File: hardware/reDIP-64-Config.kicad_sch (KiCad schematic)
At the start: 19 parts, among them J7 Conn_02x05_Odd_Even, SW1 KXT331LHS, U17 W957A8MFYA5I, U18 W25Q128JVPIM, U4 LFE5UM5G-25F-8MG285C

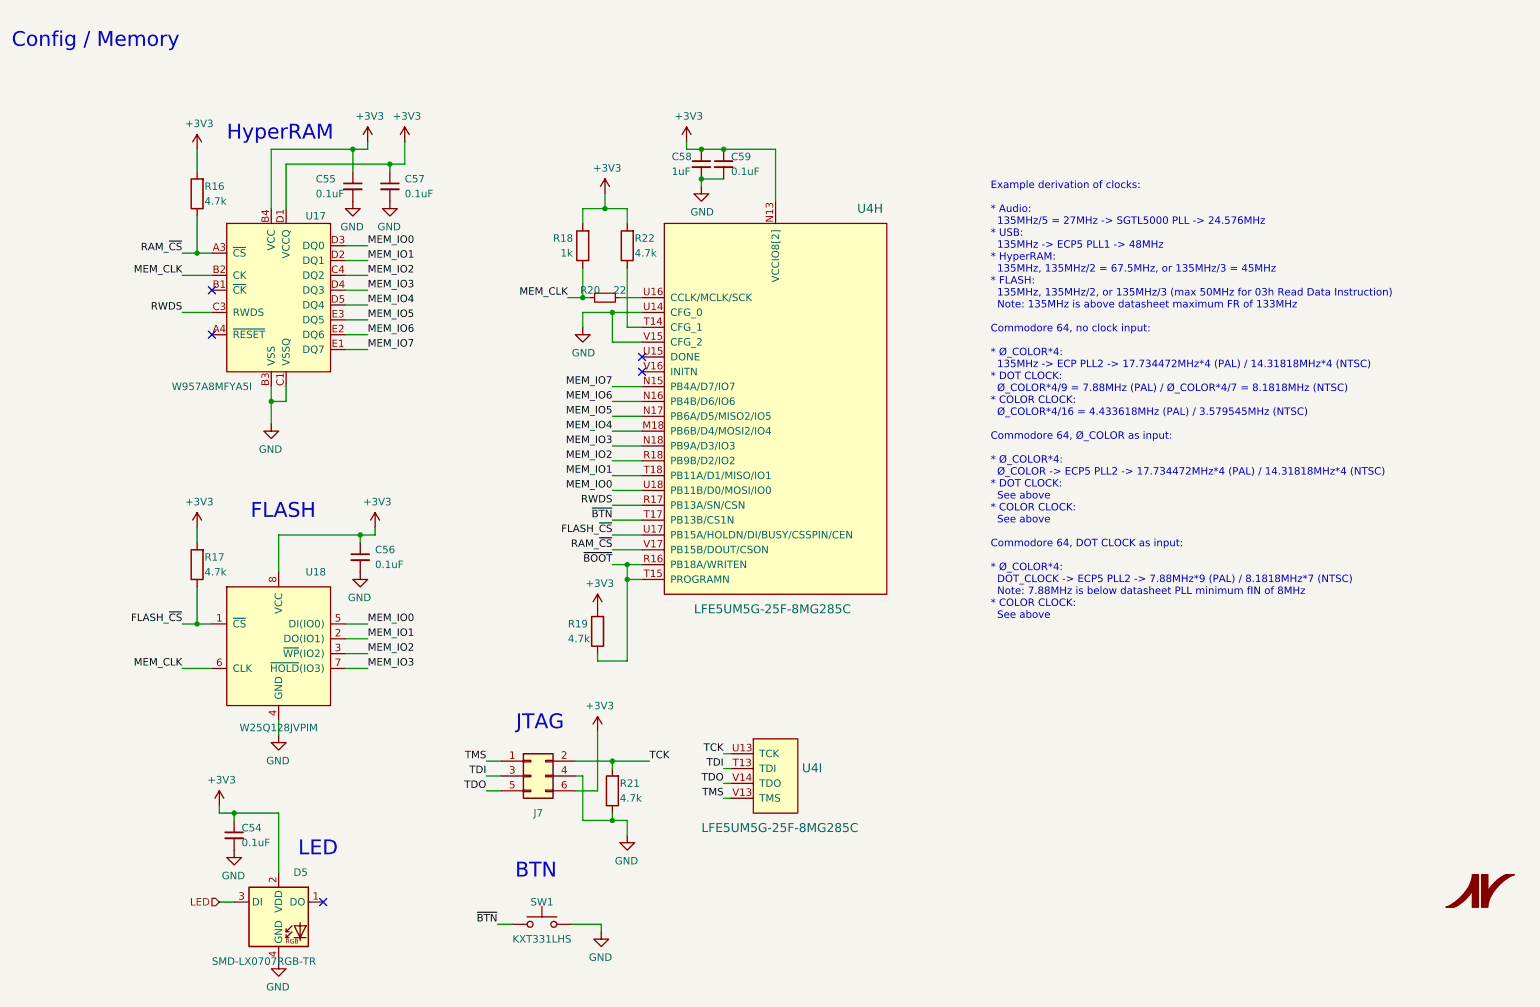
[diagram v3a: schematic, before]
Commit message: Revision 1.0
* USB receptacle replaced with GCT USB4080-03-A / HRO TYPE-C-31-M-05
* USB PD TCPC changed to PTN5110NHQ (FPF2286 has 15ms VBUS debounce time)
* Complete rework of power section
  - Over-voltage protection on VBUS (FPF2286 / FPF2495C)
  - Bidirectional VCC (2 x TPS22916)
  - Replaced EOLed buck converters with FAN53610 / FAN53611
  - Replaced EOLed LDO for ECP5 VCCAUX with NCP115AMX250TCG
  - Replaced LDO for SGTL5000 VDDA with 3.3V version
  - Added separate LDO for SGTL5000 VDDD, avoiding overvoltage on ECP5 VCC
* Bus switch changed to SN74CBT16211A, biased for level shifting
* Registered I/O for FLASH / HyperRAM clock
* Pin header changes:
  - Machined (round) pins for MOS6510 socket
  - Top only headers for additional I/O
  - Reworked pinout for VIC-II and SID
  - Removed 5V output (now available on bidirectional VCC)
  - Added GND for audio / 3.3V
  - Changed JTAG pinout to match Tag-Connect TC-LATTICE / TC-XILINX6
* Removed EXT_IN capacitors
* Button force changed from 240gf to 100gf
* Space for UL and date codes
* Black solder mask
* Silk screen updates
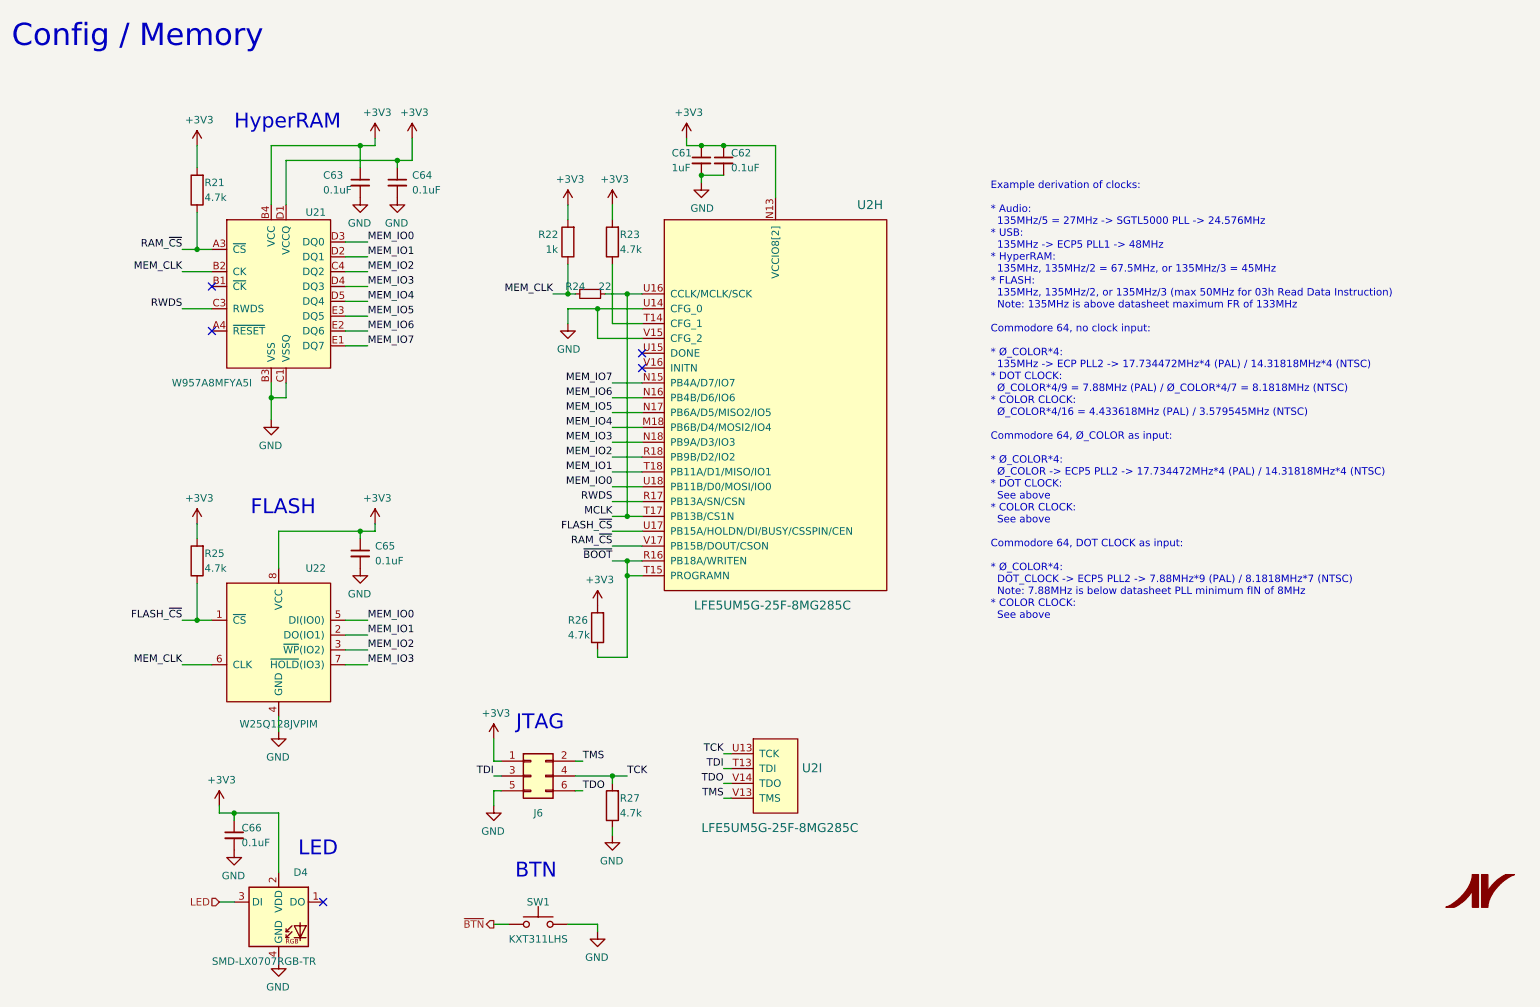
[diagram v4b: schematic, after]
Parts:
- J6: renamed from J7; Mfg Sullins -> (none); PN GRPB032VWVN-RC -> (none)
- R21: renamed from R16; PN ERJ-1GNJ472C -> ERJ1GNJ472C
- R22: renamed from R18; PN ERJ-1GNJ102C -> ERJ1GNF1001C
- R23: renamed from R22; PN ERJ-1GNJ472C -> ERJ1GNJ472C
- R24: renamed from R20; PN ERJ-1GNJ220C -> ERJ1GNJ220C
- R25: renamed from R17; PN ERJ-1GNJ472C -> ERJ1GNJ472C
- R26: renamed from R19; PN ERJ-1GNJ472C -> ERJ1GNJ472C
- R27: renamed from R21; PN ERJ-1GNJ472C -> ERJ1GNJ472C
- SW1: value KXT331LHS -> KXT311LHS; footprint Button_Switch_SMD:SW_SPST_CK_KXT3 -> CK:SW_SPST_CK_KXT3; PN KXT331LHS -> KXT311LHS
- renumbered C58 to C61, C59 to C62, C55 to C63, C57 to C64, C56 to C65, C54 to C66, D5 to D4, U4 to U2, U17 to U21, U18 to U22
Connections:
- net +3V3: now also J6.1 (Pin_1); no longer J6.6 (Pin_6)
- net GND: now also J6.5 (Pin_5); no longer J6.4 (Pin_4)
- net TCK: now also J6.4 (Pin_4); no longer J6.2 (Pin_2)
- net TDO: now also J6.6 (Pin_6); no longer J6.5 (Pin_5)
- net TMS: now also J6.2 (Pin_2); no longer J6.1 (Pin_1)
- net ~{BTN}: no longer U2.T17 (PB13B/CS1N)
- net MCLK: now reaches R24.1, U2.U16 (CCLK/MCLK/SCK)
- net MCLK: now also U2.T17 (PB13B/CS1N)
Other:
- moved on the sheet: C61, C62, C63, C64, C65, R21, R22, R23, R24, R25, R26, R27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

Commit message: Replaced socket pin headers with socket adapter
The socket adapter should hopefully *just* fit.
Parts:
- renumbered J6 to J5
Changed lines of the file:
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@@
   (symbol (lib_id "Connector_Generic:Conn_02x03_Odd_Even") (at 114.3 152.4 0) (unit 1)
     (in_bom yes) (on_board yes)
-    (property "Reference" "J6" (id 0) (at 115.57 158.75 0))
+    (property "Reference" "J5" (id 0) (at 115.57 158.75 0))
     (property "Value" "Conn_02x05_Odd_Even" (id 1) (at 115.57 144.1196 0)
       (effects (font (size 1.27 1.27)) hide)

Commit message: A few improvements
* Changed MCLK pullup to 4.7k
* A few pin swaps for cleaner routing
* Example pin headers in BOM
* Replaced reduced lifetime "mobile only" capacitors
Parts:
- C61: Notes 3.3V DC DERATED TO 1uF -> 3.3V DC DERATED TO 0.7uF; PN GRM035R60J475ME15D -> GRM033R60J225ME01D
- J5: Mfg (none) -> Sullins; PN (none) -> GRPB032VWVN-RC
- R22: value 1k -> 4.7k
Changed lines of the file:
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@@
   (title_block
     (title "reDIP 64")
-    (date "2022-04-10")
+    (date "2022-04-14")
     (rev "1.0")
     (company "Nimrod")
@@
   (symbol (lib_id "Device:R") (at 120.65 60.96 180) (unit 1)
     (in_bom yes) (on_board yes)
-    (property "Reference" "R22" (id 0) (at 115.57 59.69 0)
+    (property "Reference" "R22" (id 0) (at 121.92 59.69 0)
       (effects (font (size 1.27 1.27)) (justify right))
     )
-    (property "Value" "1k" (id 1) (at 116.84 62.23 0)
+    (property "Value" "4.7k" (id 1) (at 121.92 62.23 0)
       (effects (font (size 1.27 1.27)) (justify right))
     )
@@
       (effects (font (size 1.27 1.27)) hide)
     )
-    (property "Datasheet" "~" (id 3) (at 114.3 152.4 0)
-      (effects (font (size 1.27 1.27)) hide)
-    )
-    (property "Description" "CONN HDR SQ PIN 2x3 POS .050\" GOLD" (id 4) (at 114.3 152.4 0)
-      (effects (font (size 1.27 1.27)) hide)
-    )
-    (property "Mfg" "" (id 5) (at 114.3 152.4 0)
-      (effects (font (size 1.27 1.27)) hide)
-    )
-    (property "PN" "" (id 6) (at 114.3 152.4 0)
+    (property "Datasheet" "https://s3.amazonaws.com/catalogspreads-pdf/PAGE94-95%20.050%20MALE%20HDR%20ST%20RA%20SMT.pdf" (id 3) (at 114.3 152.4 0)
+      (effects (font (size 1.27 1.27)) hide)
+    )
+    (property "Description" "CONN HDR SQ PIN 2x3 POS .050\" GOLD MATING 3mm" (id 4) (at 114.3 152.4 0)
+      (effects (font (size 1.27 1.27)) hide)
+    )
+    (property "Mfg" "Sullins" (id 5) (at 114.3 152.4 0)
+      (effects (font (size 1.27 1.27)) hide)
+    )
+    (property "PN" "GRPB032VWVN-RC" (id 6) (at 114.3 152.4 0)
       (effects (font (size 1.27 1.27)) hide)
     )
@@
       (effects (font (size 1.27 1.27)) hide)
     )
-    (property "Datasheet" "https://www.murata.com/products/productdetail.aspx?partno=GRM035R60J475ME15D" (id 3) (at 143.51 46.99 0)
+    (property "Datasheet" "https://www.murata.com/products/productdetail.aspx?partno=GRM033R60J225ME01D" (id 3) (at 143.51 46.99 0)
       (effects (font (size 1.27 1.27)) hide)
     )
@@
       (effects (font (size 1.27 1.27)) hide)
     )
-    (property "PN" "GRM035R60J475ME15D" (id 5) (at 143.51 46.99 0)
-      (effects (font (size 1.27 1.27)) hide)
-    )
-    (property "Description" "CAP CER 4.7uF 6.3V 20% X5R 0201" (id 6) (at 143.51 46.99 0)
-      (effects (font (size 1.27 1.27)) hide)
-    )
-    (property "Notes" "3.3V DC DERATED TO 1uF" (id 7) (at 143.51 46.99 0)
-      (effects (font (size 1.27 1.27)) hide)
-    )
+    (property "PN" "GRM033R60J225ME01D" (id 5) (at 143.51 46.99 0)
+      (effects (font (size 1.27 1.27)) hide)
+    )
+    (property "Description" "CAP CER 2.2uF 6.3V 20% X5R 0201" (id 6) (at 143.51 46.99 0)
+      (effects (font (size 1.27 1.27)) hide)
+    )
+    (property "Notes" "3.3V DC DERATED TO 0.7uF" (id 7) (at 143.51 46.99 0)
+      (effects (font (size 1.27 1.27)) hide)
+    )

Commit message: BOM correction, silk screen update
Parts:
- R22: PN ERJ1GNF1001C -> ERJ1GNJ472C
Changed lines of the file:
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@@
       (effects (font (size 1.27 1.27)) hide)
     )
-    (property "Datasheet" "https://industrial.panasonic.com/ww/products/pt/general-purpose-chip-resistors/models/ERJ1GNF1001C" (id 3) (at 120.65 60.96 0)
+    (property "Datasheet" "https://industrial.panasonic.com/ww/products/pt/general-purpose-chip-resistors/models/ERJ1GNJ472C" (id 3) (at 120.65 60.96 0)
       (effects (font (size 1.27 1.27)) hide)
     )
@@
       (effects (font (size 1.27 1.27)) hide)
     )
-    (property "PN" "ERJ1GNF1001C" (id 5) (at 120.65 60.96 0)
+    (property "PN" "ERJ1GNJ472C" (id 5) (at 120.65 60.96 0)
       (effects (font (size 1.27 1.27)) hide)
     )
-    (property "Description" "RES 1kΩ 50mW 1% 0201" (id 6) (at 120.65 60.96 0)
+    (property "Description" "RES 4.7kΩ 50mW 5% 0201" (id 6) (at 120.65 60.96 0)
       (effects (font (size 1.27 1.27)) hide)
     )
